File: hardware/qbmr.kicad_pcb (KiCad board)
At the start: 2 copper layers, 61.7 x 46.8 mm, 35 parts, among them P1 CONN_01X01, P10 GND, P2 CONN_01X01, P3 CONN_01X01, P4 CONN_01X01, P5 CONN_01X01, P6 CONN_01X01, P7 CONN_01X01, P8 CONN_01X01, P9 VCC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

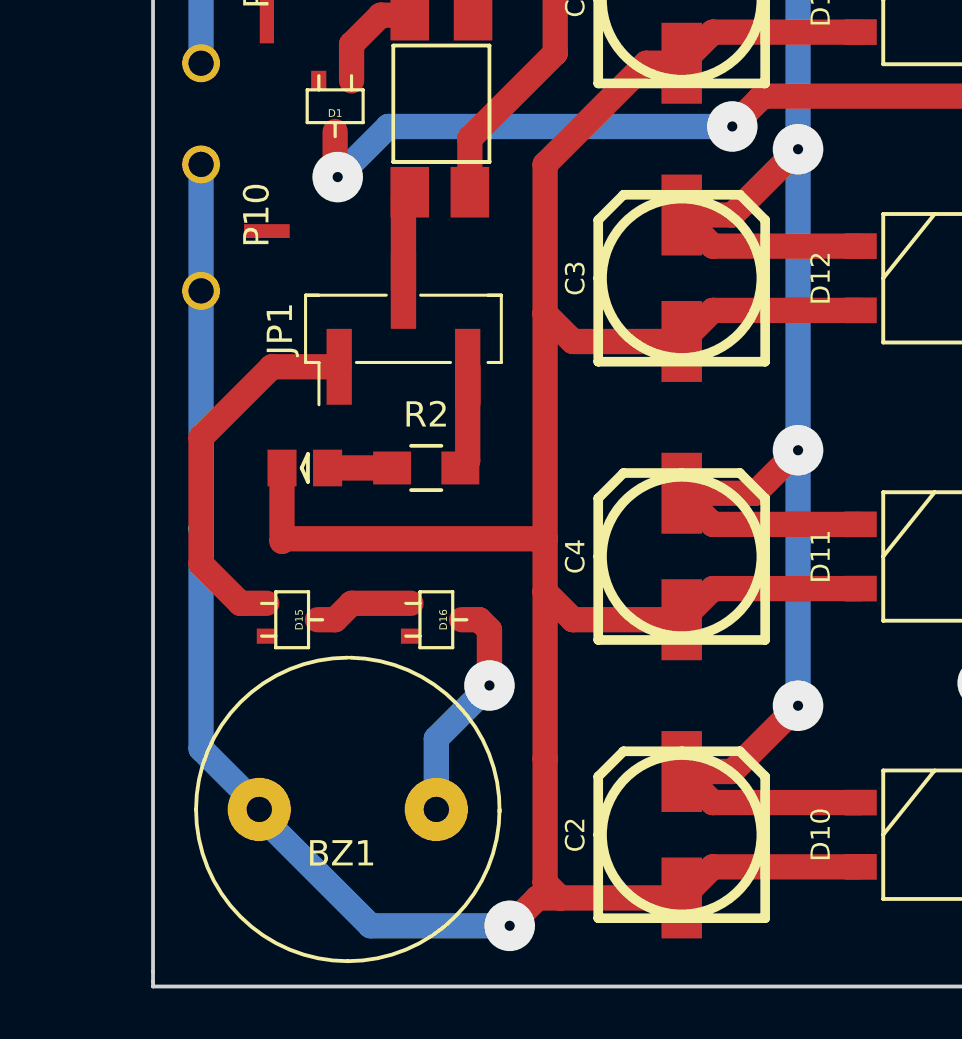
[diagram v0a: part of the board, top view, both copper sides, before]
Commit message: Updating schematics.
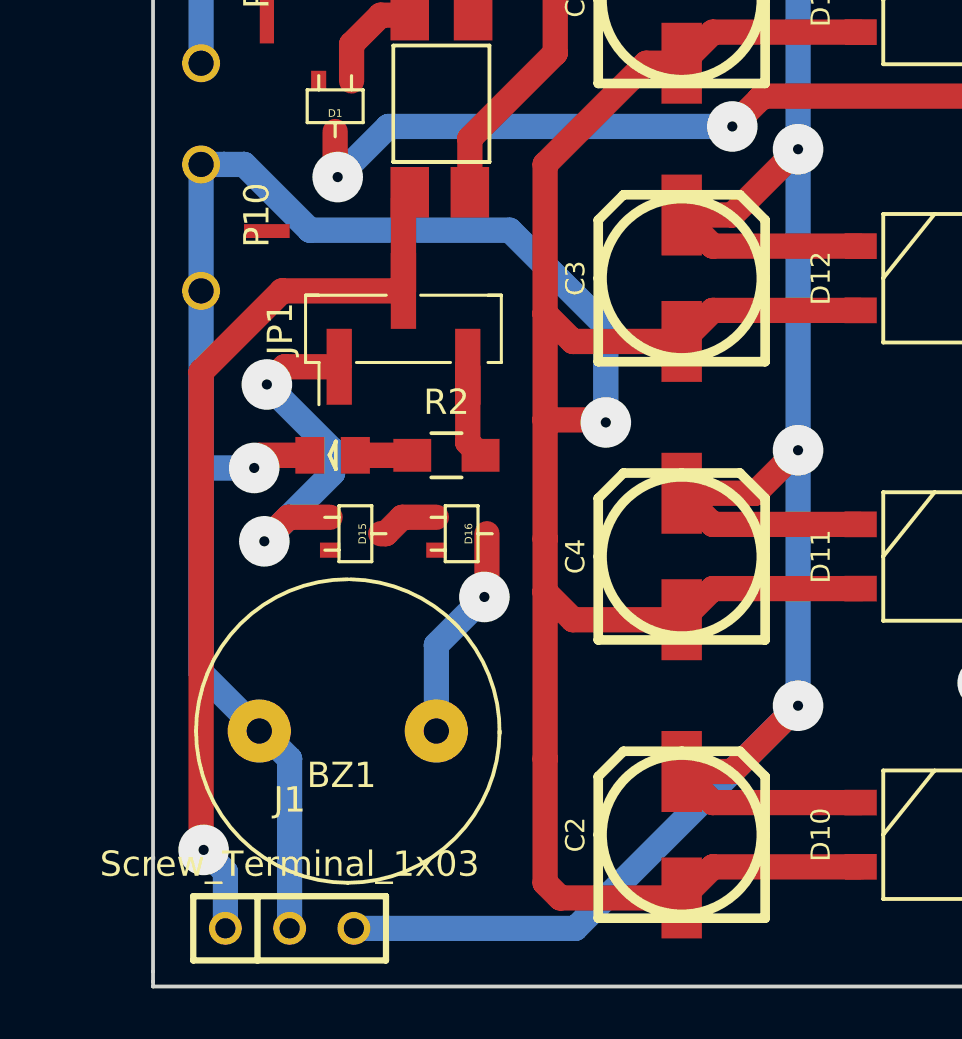
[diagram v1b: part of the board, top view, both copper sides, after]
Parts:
- added J1: Screw_Terminal_1x03, ChristianLerche/LercheTech_KiCAD/LercheTech.pretty:Lerche_3P_2.54mm, F.Cu at (143.5, 82.7)
- moved D15 4.22 mm to (146.1, 67.1)
- moved D16 3.54 mm to (150.3, 67.1)
- moved BZ1 3.10 mm to (145.8, 74.9)
- moved D14 1.21 mm to (145.2, 64.0)
- moved R2 0.94 mm to (149.7, 64.0)
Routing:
- net Net-(J1-Pad1): track 4.00 -> 35.7 mm, vias 0 -> 1
- net VCC: track 129.1 -> 150.3 mm
- net GND: track 137.3 -> 144.8 mm, vias 1 -> 2
- net Net-(D15-Pad1): track 3.97 -> 2.47 mm
- net Net-(BZ1-Pad1): track 9.23 -> 8.63 mm
- net Net-(D15-Pad2): track 14.9 -> 14.5 mm, vias 0 -> 2

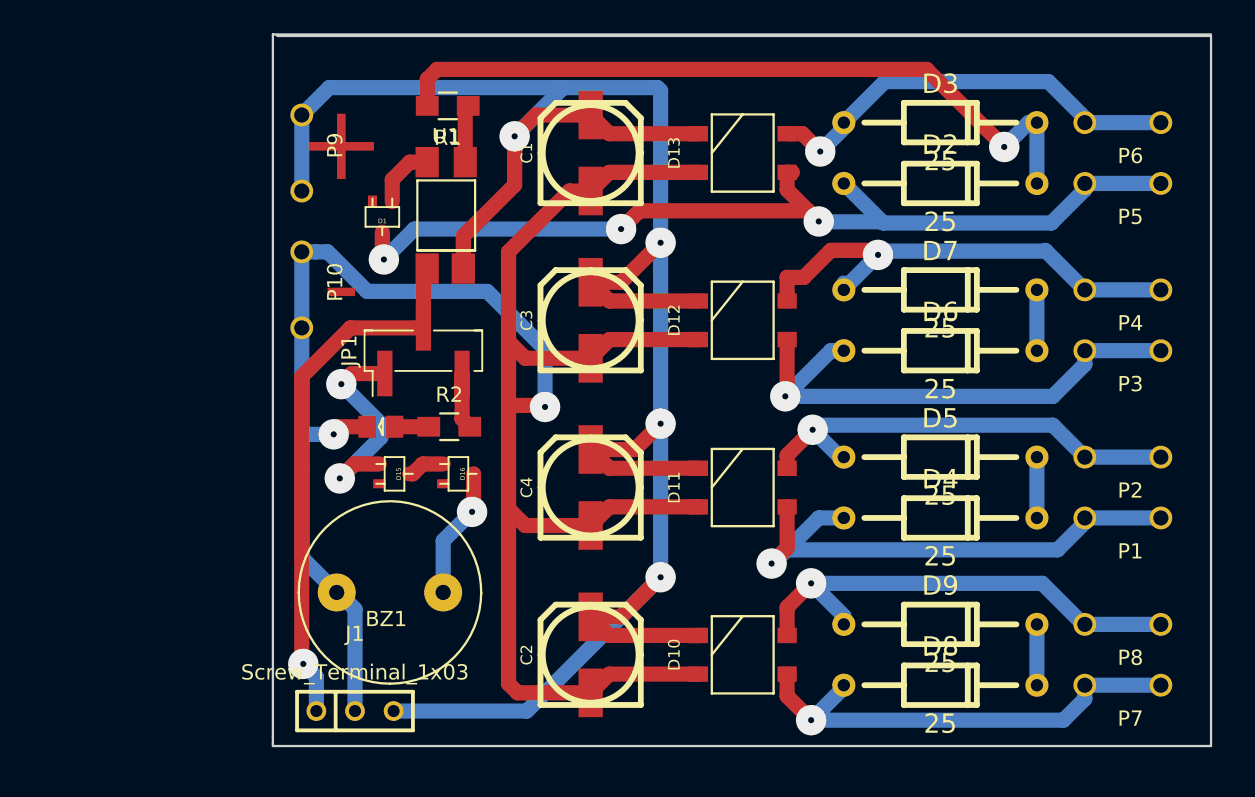
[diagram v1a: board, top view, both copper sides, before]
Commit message: Switching to use a microcontroller for voltage measurements.
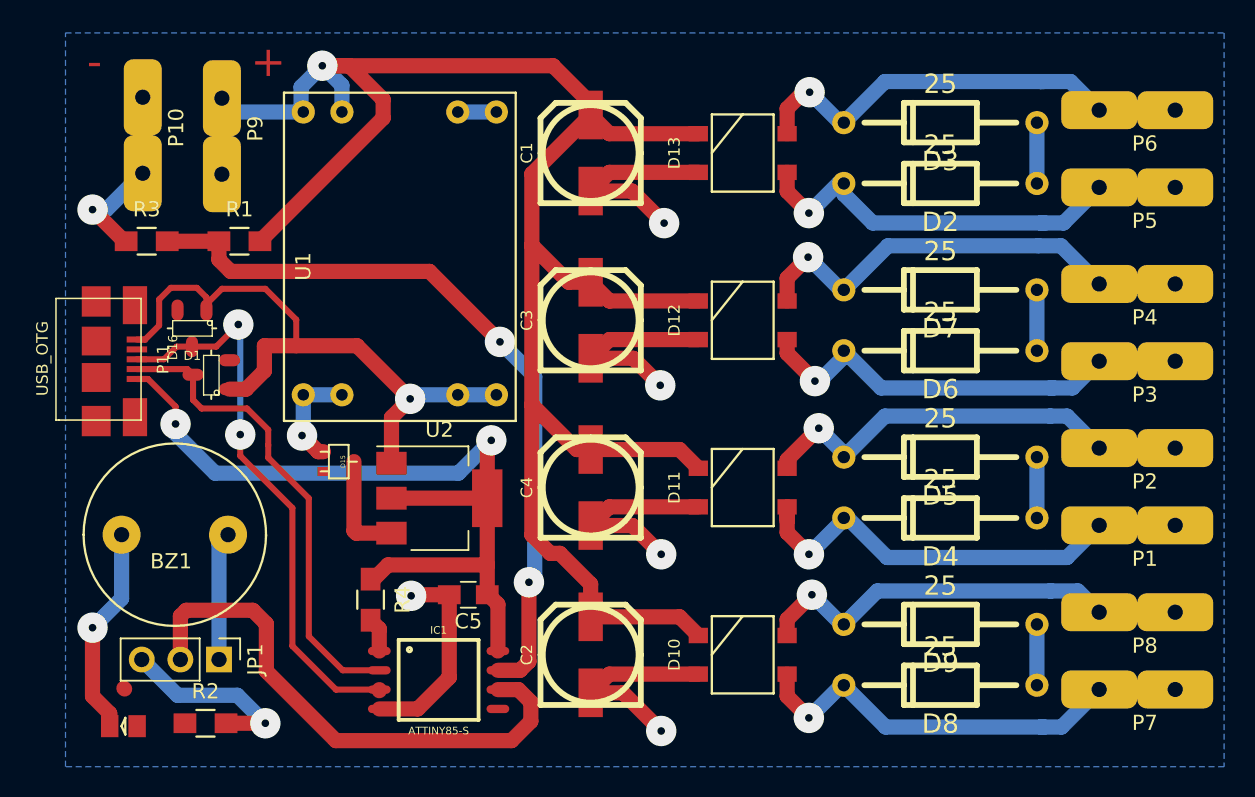
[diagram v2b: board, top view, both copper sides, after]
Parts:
- removed J1: Screw_Terminal_1x03, ChristianLerche/LercheTech_KiCAD/LercheTech.pretty:Lerche_3P_2.54mm
- added C5: 0.1u, Capacitors_SMD:C_0805_HandSoldering, F.Cu at (150.9, 75.0)
- added IC1: ATTINY85-S, brunoeagle/kicad-open-modules:SOIC8, F.Cu at (149.0, 80.7)
- added P11: USB_OTG, qbmr:MICRO-B_USB-INVERTED, F.Cu at (125.0, 59.6)
- added R3: 200, apexelectrix/apex-smd-resistors.pretty:R_0805_HandSoldering, F.Cu at (129.8, 51.8)
- added R4: 10k, apexelectrix/apex-smd-resistors.pretty:R_0805_HandSoldering, F.Cu at (144.5, 75.4)
- added U2: AP111750, TO_SOT_Packages_SMD:SOT-223, F.Cu at (149.1, 68.7)
- D1, D16: value D -> 3.6; footprint qbmr:SOT323_diode -> qbmr:DIODE-SOT-23-3
- D2, D3, D4, D5, D6, D7, D8, D9: footprint fruchti/fruchtilib/mod/do.pretty:DO204AL_500 -> qbmr:DO204AL_500
- JP1: footprint KiCad/Pin_Headers.pretty:Pin_Header_Straight_1x03_Pitch2.54mm_SMD_Pin1Left -> KiCad/Pin_Headers.pretty:Pin_Header_Straight_1x03_Pitch2.54mm
- U1: value TLP187 -> MP1584EN; footprint qbmr:SMD-OPTOCOUPLER -> qbmr:MP1584EN
- moved D14 26.0 mm to (128.3, 83.7)
- moved R2 25.2 mm to (133.7, 83.5)
- moved JP1 24.4 mm to (134.6, 79.3), turned to 270 degrees
- moved D16 20.0 mm to (132.8, 57.5), turned to 180 degrees
- moved R1 16.3 mm to (135.9, 51.8), turned to 0 degrees
- moved D1 15.3 mm to (134.0, 60.6), turned to 90 degrees
- moved BZ1 14.7 mm to (131.7, 71.1)
- moved P10 14.6 mm to (129.5, 44.8)
- moved U1 7.56 mm to (152.8, 43.3), turned to 270 degrees
- moved P9 5.37 mm to (134.7, 44.9)
- moved D15 3.76 mm to (142.4, 66.3)
- moved P6 1.25 mm to (194.9, 43.2)
- moved P8 1.24 mm to (194.9, 76.2)
- moved P3 1.17 mm to (194.9, 59.7)
- moved P2 1.12 mm to (194.9, 65.4)
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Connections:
- D1 pad 1: Net-(D1-Pad1) -> USBD-
- D1 pad 2: Net-(D1-Pad2) -> GND
- D13 pad 3: Net-(D1-Pad1) -> Net-(D13-Pad3)
- D16 pad 1: Net-(BZ1-Pad1) -> USBD+
- D16 pad 2: Net-(D15-Pad1) -> GND
- D2 pad 1: Net-(D1-Pad1) -> Net-(D13-Pad3)
- JP1 pad 1: Net-(D15-Pad2) -> Net-(BZ1-Pad1)
- JP1 pad 2: Net-(J1-Pad1) -> Net-(IC1-Pad6)
- P5 pad 1: Net-(D1-Pad1) -> Net-(D13-Pad3)
- R1 pad 1: Net-(R1-Pad1) -> Net-(IC1-Pad7)
- R1 pad 2: Net-(D2-Pad2) -> VCC
- U1 pad 1: Net-(R1-Pad1) -> GND
- U1 pad 3: Net-(D1-Pad2) -> GND
- U1 pad 4: Net-(J1-Pad1) -> Net-(D15-Pad2)
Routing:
- net Net-(D1-Pad1): track 63.9 -> 0.00 mm, vias 3 -> 0
- net VUSB: track 0.00 -> 57.1 mm, vias 0 -> 2
- net Net-(IC1-Pad7): track 0.00 -> 49.7 mm, vias 0 -> 2
- net Net-(D2-Pad2): track 49.3 -> 4.00 mm, vias 1 -> 0
- net USBD+: track 0.00 -> 37.2 mm, vias 0 -> 2
- net Net-(IC1-Pad6): track 0.00 -> 35.7 mm
- net Net-(J1-Pad1): track 35.7 -> 0.00 mm, vias 1 -> 0
- net USBD-: track 0.00 -> 31.5 mm
- net Net-(D13-Pad3): track 0.00 -> 30.9 mm, vias 0 -> 1
- net VCC: track 150.3 -> 132.1 mm, vias 4 -> 1
- net GND: track 144.8 -> 133.0 mm, vias 2 -> 8
- net Net-(D15-Pad2): track 14.5 -> 7.11 mm, vias 2 -> 1
- net Net-(JP1-Pad3): track 5.15 -> 12.5 mm, vias 0 -> 1
- net Net-(D12-Pad3): track 35.7 -> 30.2 mm
- net Net-(D11-Pad3): track 37.4 -> 32.0 mm
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- added copper zone on B.Cu, net GND
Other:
- board outline removed
- net class Default: clearance 0.5 -> 0.2; via_drill 0.4 -> 0.5
- rule trace_clearance: 0.5 -> 0.2
